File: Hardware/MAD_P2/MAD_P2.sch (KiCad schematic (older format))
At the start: 51 parts, among them U1 P2X8C4M64P-REF, Y1 20MHz

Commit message: added optional sd card socket for data
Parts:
- added SW?: Switch_SW_Push, symbol Power-cache:Switch_SW_Push
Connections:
- net GND: now also SW?.2
- net RESET: now also SW?.1
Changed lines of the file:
@@
 Text Notes 2950 2050 0    129  ~ 0
 Propeller 2
+$Comp
+L Power-cache:Switch_SW_Push SW?
+U 1 1 61238802
+P 3600 6750
+F 0 "SW?" H 3600 7035 50  0000 C CNN
+F 1 "Switch_SW_Push" H 3600 6944 50  0000 C CNN
+F 2 "" H 3600 6950 50  0001 C CNN
+F 3 "" H 3600 6950 50  0001 C CNN
+	1    3600 6750
+	1    0    0    -1
+$EndComp
+Text Label 3400 6750 2    50   ~ 0
+RESET
+$Comp
+L power:GND #PWR?
+U 1 1 6123970E
+P 3800 6750
+F 0 "#PWR?" H 3800 6500 50  0001 C CNN
+F 1 "GND" H 3805 6577 50  0000 C CNN
+F 2 "" H 3800 6750 50  0001 C CNN
+F 3 "" H 3800 6750 50  0001 C CNN
+	1    3800 6750
+	0    -1   -1   0
+$EndComp
 $EndSCHEMATC

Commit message: revising pcb layout
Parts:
- SW1: renamed from SW?; footprint (none) -> Button_Switch_THT:SW_PUSH_6mm
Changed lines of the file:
@@
 Propeller 2
 $Comp
-L Power-cache:Switch_SW_Push SW?
+L Power-cache:Switch_SW_Push SW1
 U 1 1 61238802
 P 3600 6750
-F 0 "SW?" H 3600 7035 50  0000 C CNN
+F 0 "SW1" H 3600 7035 50  0000 C CNN
 F 1 "Switch_SW_Push" H 3600 6944 50  0000 C CNN
-F 2 "" H 3600 6950 50  0001 C CNN
+F 2 "Button_Switch_THT:SW_PUSH_6mm" H 3600 6950 50  0001 C CNN
 F 3 "" H 3600 6950 50  0001 C CNN
 	1    3600 6750
@@
 RESET
 $Comp
-L power:GND #PWR?
+L power:GND #PWR0101
 U 1 1 6123970E
 P 3800 6750
-F 0 "#PWR?" H 3800 6500 50  0001 C CNN
+F 0 "#PWR0101" H 3800 6500 50  0001 C CNN
 F 1 "GND" H 3805 6577 50  0000 C CNN
 F 2 "" H 3800 6750 50  0001 C CNN

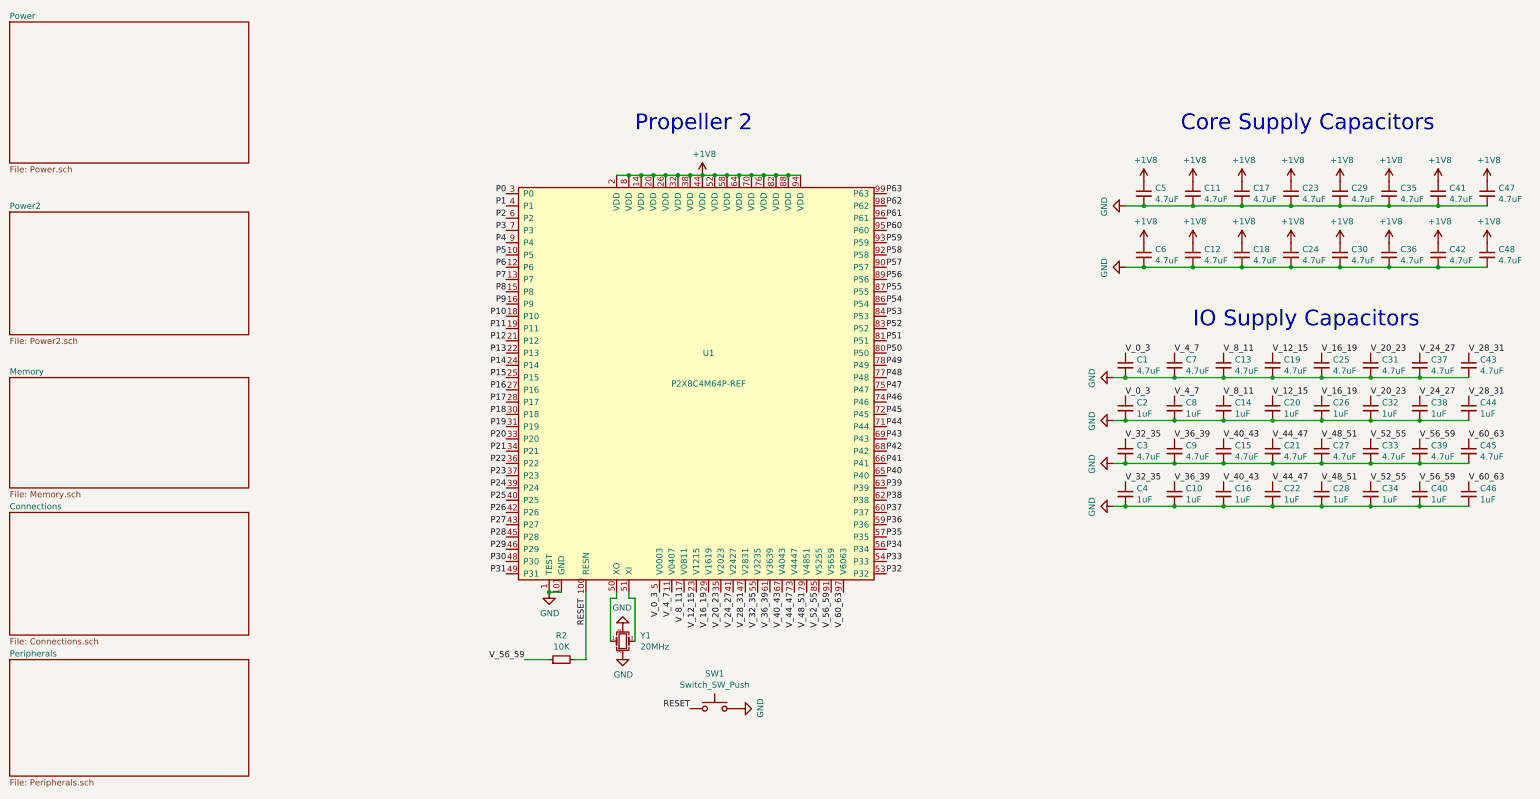
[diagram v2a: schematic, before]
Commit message: routed adc
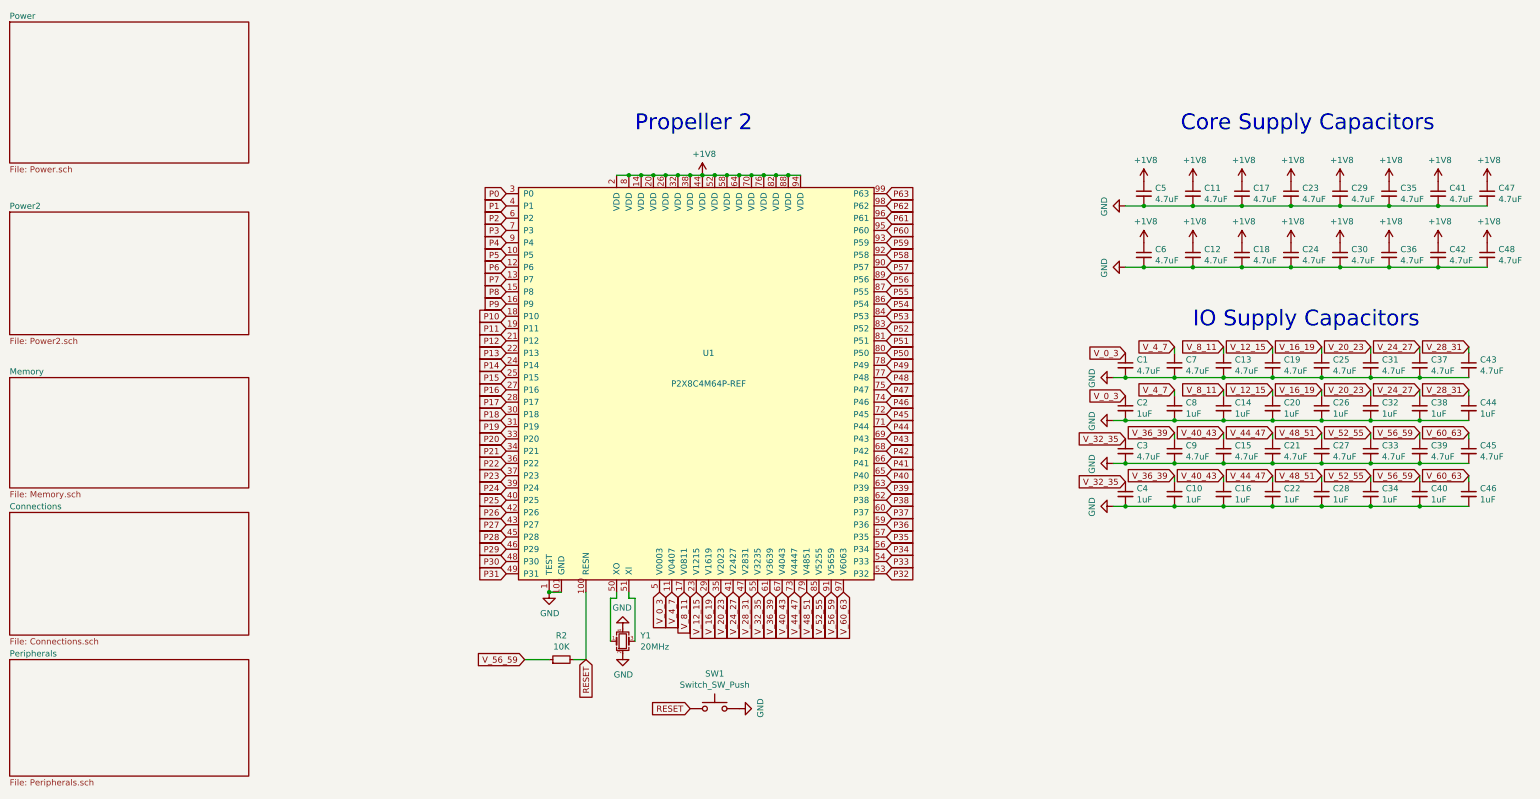
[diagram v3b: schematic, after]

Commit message: completed BOM with digikey and LSCS parts
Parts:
- C1, C11, C12, C13, C15, C17, C18, C19, C21, C23, C24, C25, C27, C29, C3, C30, C31, C33, C35, C36, C37, C39, C41, C42, C43, C45, C47, C48, C5, C6, C7, C9: LCSC (none) -> C19666; TYPE (none) -> BASIC
- C10, C14, C16, C2, C20, C22, C26, C28, C32, C34, C38, C4, C40, C44, C46, C8: LCSC (none) -> C15849; TYPE (none) -> BASIC
- R2: LCSC (none) -> C25804; TYPE (none) -> BASIC
- SW1: TYPE (none) -> NA
- U1: DIGIKEY (none) -> 149-P2X8C4M64P-ND; TYPE (none) -> DIGIKEY
- Y1: LCSC (none) -> C110936; TYPE (none) -> EXT

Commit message: added more functionality to JSON for motion quartet, motion set, motion profiles, machine profile, and more
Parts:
- C1, C10, C11, C12, C13, C14, C15, C16, C17, C18, C19, C2, C20, C21, C22, C23, C24, C25, C26, C27, C28, C29, C3, C30, C31, C32, C33, C34, C35, C36, C37, C38, C39, C4, C40, C41, C42, C43, C44, C45, C46, C47, C48, C5, C6, C7, C8, C9, R2: ASSEMBLED (none) -> YES
- U1, Y1: ASSEMBLED (none) -> NO
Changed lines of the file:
@@
 F 4 "149-P2X8C4M64P-ND" H 3550 4150 50  0001 C CNN "DIGIKEY"
 F 5 "DIGIKEY" H 3550 4150 50  0001 C CNN "TYPE"
+F 6 "NO" H 3550 4150 50  0001 C CNN "ASSEMBLED"
 	1    3550 4150
 	1    0    0    -1
@@
 F 4 "C110936" H 2850 6200 50  0001 C CNN "LCSC"
 F 5 "EXT" H 2850 6200 50  0001 C CNN "TYPE"
+F 6 "NO" H 2850 6200 50  0001 C CNN "ASSEMBLED"
 	1    2850 6200
 	1    0    0    -1
@@
 F 4 "C19666" H 7100 2550 50  0001 C CNN "LCSC"
 F 5 "BASIC" H 7100 2550 50  0001 C CNN "TYPE"
+F 6 "YES" H 7100 2550 50  0001 C CNN "ASSEMBLED"
 	1    7100 2550
 	1    0    0    -1
@@
 F 4 "C19666" H 7500 2550 50  0001 C CNN "LCSC"
 F 5 "BASIC" H 7500 2550 50  0001 C CNN "TYPE"
+F 6 "YES" H 7500 2550 50  0001 C CNN "ASSEMBLED"
 	1    7500 2550
 	1    0    0    -1
@@
 F 4 "C19666" H 7900 2550 50  0001 C CNN "LCSC"
 F 5 "BASIC" H 7900 2550 50  0001 C CNN "TYPE"
+F 6 "YES" H 7900 2550 50  0001 C CNN "ASSEMBLED"
 	1    7900 2550
 	1    0    0    -1
@@
 F 4 "C19666" H 8300 2550 50  0001 C CNN "LCSC"
 F 5 "BASIC" H 8300 2550 50  0001 C CNN "TYPE"
+F 6 "YES" H 8300 2550 50  0001 C CNN "ASSEMBLED"
 	1    8300 2550
 	1    0    0    -1
@@
 F 4 "C19666" H 8700 2550 50  0001 C CNN "LCSC"
 F 5 "BASIC" H 8700 2550 50  0001 C CNN "TYPE"
+F 6 "YES" H 8700 2550 50  0001 C CNN "ASSEMBLED"
 	1    8700 2550
 	1    0    0    -1
@@
 F 4 "C19666" H 9100 2550 50  0001 C CNN "LCSC"
 F 5 "BASIC" H 9100 2550 50  0001 C CNN "TYPE"
+F 6 "YES" H 9100 2550 50  0001 C CNN "ASSEMBLED"
 	1    9100 2550
 	1    0    0    -1
@@
 F 4 "C19666" H 9500 2550 50  0001 C CNN "LCSC"
 F 5 "BASIC" H 9500 2550 50  0001 C CNN "TYPE"
+F 6 "YES" H 9500 2550 50  0001 C CNN "ASSEMBLED"
 	1    9500 2550
 	1    0    0    -1
@@
 F 4 "C19666" H 9900 2550 50  0001 C CNN "LCSC"
 F 5 "BASIC" H 9900 2550 50  0001 C CNN "TYPE"
+F 6 "YES" H 9900 2550 50  0001 C CNN "ASSEMBLED"
 	1    9900 2550
 	1    0    0    -1
@@
 F 4 "C19666" H 7100 3050 50  0001 C CNN "LCSC"
 F 5 "BASIC" H 7100 3050 50  0001 C CNN "TYPE"
+F 6 "YES" H 7100 3050 50  0001 C CNN "ASSEMBLED"
 	1    7100 3050
 	1    0    0    -1
@@
 F 4 "C19666" H 7500 3050 50  0001 C CNN "LCSC"
 F 5 "BASIC" H 7500 3050 50  0001 C CNN "TYPE"
+F 6 "YES" H 7500 3050 50  0001 C CNN "ASSEMBLED"
 	1    7500 3050
 	1    0    0    -1
@@
 F 4 "C19666" H 7900 3050 50  0001 C CNN "LCSC"
 F 5 "BASIC" H 7900 3050 50  0001 C CNN "TYPE"
+F 6 "YES" H 7900 3050 50  0001 C CNN "ASSEMBLED"
 	1    7900 3050
 	1    0    0    -1
@@
 F 4 "C19666" H 8300 3050 50  0001 C CNN "LCSC"
 F 5 "BASIC" H 8300 3050 50  0001 C CNN "TYPE"
+F 6 "YES" H 8300 3050 50  0001 C CNN "ASSEMBLED"
 	1    8300 3050
 	1    0    0    -1
@@
 F 4 "C19666" H 8700 3050 50  0001 C CNN "LCSC"
 F 5 "BASIC" H 8700 3050 50  0001 C CNN "TYPE"
+F 6 "YES" H 8700 3050 50  0001 C CNN "ASSEMBLED"
 	1    8700 3050
 	1    0    0    -1
@@
 F 4 "C19666" H 9100 3050 50  0001 C CNN "LCSC"
 F 5 "BASIC" H 9100 3050 50  0001 C CNN "TYPE"
+F 6 "YES" H 9100 3050 50  0001 C CNN "ASSEMBLED"
 	1    9100 3050
 	1    0    0    -1
@@
 F 4 "C19666" H 9500 3050 50  0001 C CNN "LCSC"
 F 5 "BASIC" H 9500 3050 50  0001 C CNN "TYPE"
+F 6 "YES" H 9500 3050 50  0001 C CNN "ASSEMBLED"
 	1    9500 3050
 	1    0    0    -1
@@
 F 4 "C19666" H 9900 3050 50  0001 C CNN "LCSC"
 F 5 "BASIC" H 9900 3050 50  0001 C CNN "TYPE"
+F 6 "YES" H 9900 3050 50  0001 C CNN "ASSEMBLED"
 	1    9900 3050
 	1    0    0    -1
@@
 F 4 "C19666" H 6950 3950 50  0001 C CNN "LCSC"
 F 5 "BASIC" H 6950 3950 50  0001 C CNN "TYPE"
+F 6 "YES" H 6950 3950 50  0001 C CNN "ASSEMBLED"
 	1    6950 3950
 	1    0    0    -1
@@
 F 4 "C19666" H 7350 3950 50  0001 C CNN "LCSC"
 F 5 "BASIC" H 7350 3950 50  0001 C CNN "TYPE"
+F 6 "YES" H 7350 3950 50  0001 C CNN "ASSEMBLED"
 	1    7350 3950
 	1    0    0    -1
@@
 F 4 "C19666" H 7750 3950 50  0001 C CNN "LCSC"
 F 5 "BASIC" H 7750 3950 50  0001 C CNN "TYPE"
+F 6 "YES" H 7750 3950 50  0001 C CNN "ASSEMBLED"
 	1    7750 3950
 	1    0    0    -1
@@
 F 4 "C19666" H 8150 3950 50  0001 C CNN "LCSC"
 F 5 "BASIC" H 8150 3950 50  0001 C CNN "TYPE"
+F 6 "YES" H 8150 3950 50  0001 C CNN "ASSEMBLED"
 	1    8150 3950
 	1    0    0    -1
@@
 F 4 "C19666" H 8550 3950 50  0001 C CNN "LCSC"
 F 5 "BASIC" H 8550 3950 50  0001 C CNN "TYPE"
+F 6 "YES" H 8550 3950 50  0001 C CNN "ASSEMBLED"
 	1    8550 3950
 	1    0    0    -1
@@
 F 4 "C19666" H 8950 3950 50  0001 C CNN "LCSC"
 F 5 "BASIC" H 8950 3950 50  0001 C CNN "TYPE"
+F 6 "YES" H 8950 3950 50  0001 C CNN "ASSEMBLED"
 	1    8950 3950
 	1    0    0    -1
@@
 F 4 "C19666" H 9350 3950 50  0001 C CNN "LCSC"
 F 5 "BASIC" H 9350 3950 50  0001 C CNN "TYPE"
+F 6 "YES" H 9350 3950 50  0001 C CNN "ASSEMBLED"
 	1    9350 3950
 	1    0    0    -1
@@
 F 4 "C19666" H 9750 3950 50  0001 C CNN "LCSC"
 F 5 "BASIC" H 9750 3950 50  0001 C CNN "TYPE"
+F 6 "YES" H 9750 3950 50  0001 C CNN "ASSEMBLED"
 	1    9750 3950
 	1    0    0    -1
@@
 F 4 "C19666" H 6950 4650 50  0001 C CNN "LCSC"
 F 5 "BASIC" H 6950 4650 50  0001 C CNN "TYPE"
+F 6 "YES" H 6950 4650 50  0001 C CNN "ASSEMBLED"
 	1    6950 4650
 	1    0    0    -1
@@
 F 4 "C19666" H 7350 4650 50  0001 C CNN "LCSC"
 F 5 "BASIC" H 7350 4650 50  0001 C CNN "TYPE"
+F 6 "YES" H 7350 4650 50  0001 C CNN "ASSEMBLED"
 	1    7350 4650
 	1    0    0    -1
@@
 F 4 "C19666" H 7750 4650 50  0001 C CNN "LCSC"
 F 5 "BASIC" H 7750 4650 50  0001 C CNN "TYPE"
+F 6 "YES" H 7750 4650 50  0001 C CNN "ASSEMBLED"
 	1    7750 4650
 	1    0    0    -1
@@
 F 4 "C19666" H 8150 4650 50  0001 C CNN "LCSC"
 F 5 "BASIC" H 8150 4650 50  0001 C CNN "TYPE"
+F 6 "YES" H 8150 4650 50  0001 C CNN "ASSEMBLED"
 	1    8150 4650
 	1    0    0    -1
@@
 F 4 "C19666" H 8550 4650 50  0001 C CNN "LCSC"
 F 5 "BASIC" H 8550 4650 50  0001 C CNN "TYPE"
+F 6 "YES" H 8550 4650 50  0001 C CNN "ASSEMBLED"
 	1    8550 4650
 	1    0    0    -1
@@
 F 4 "C19666" H 8950 4650 50  0001 C CNN "LCSC"
 F 5 "BASIC" H 8950 4650 50  0001 C CNN "TYPE"
+F 6 "YES" H 8950 4650 50  0001 C CNN "ASSEMBLED"
 	1    8950 4650
 	1    0    0    -1
@@
 F 4 "C19666" H 9350 4650 50  0001 C CNN "LCSC"
 F 5 "BASIC" H 9350 4650 50  0001 C CNN "TYPE"
+F 6 "YES" H 9350 4650 50  0001 C CNN "ASSEMBLED"
 	1    9350 4650
 	1    0    0    -1
@@
 F 4 "C19666" H 9750 4650 50  0001 C CNN "LCSC"
 F 5 "BASIC" H 9750 4650 50  0001 C CNN "TYPE"
+F 6 "YES" H 9750 4650 50  0001 C CNN "ASSEMBLED"
 	1    9750 4650
 	1    0    0    -1
@@
 F 4 "C15849" H 6950 5000 50  0001 C CNN "LCSC"
 F 5 "BASIC" H 6950 5000 50  0001 C CNN "TYPE"
+F 6 "YES" H 6950 5000 50  0001 C CNN "ASSEMBLED"
 	1    6950 5000
 	1    0    0    -1
@@
 F 4 "C15849" H 7350 5000 50  0001 C CNN "LCSC"
 F 5 "BASIC" H 7350 5000 50  0001 C CNN "TYPE"
+F 6 "YES" H 7350 5000 50  0001 C CNN "ASSEMBLED"
 	1    7350 5000
 	1    0    0    -1
@@
 F 4 "C15849" H 7750 5000 50  0001 C CNN "LCSC"
 F 5 "BASIC" H 7750 5000 50  0001 C CNN "TYPE"
+F 6 "YES" H 7750 5000 50  0001 C CNN "ASSEMBLED"
 	1    7750 5000
 	1    0    0    -1
@@
 F 4 "C15849" H 8150 5000 50  0001 C CNN "LCSC"
 F 5 "BASIC" H 8150 5000 50  0001 C CNN "TYPE"
+F 6 "YES" H 8150 5000 50  0001 C CNN "ASSEMBLED"
 	1    8150 5000
 	1    0    0    -1
@@
 F 4 "C15849" H 8550 5000 50  0001 C CNN "LCSC"
 F 5 "BASIC" H 8550 5000 50  0001 C CNN "TYPE"
+F 6 "YES" H 8550 5000 50  0001 C CNN "ASSEMBLED"
 	1    8550 5000
 	1    0    0    -1
@@
 F 4 "C15849" H 8950 5000 50  0001 C CNN "LCSC"
 F 5 "BASIC" H 8950 5000 50  0001 C CNN "TYPE"
+F 6 "YES" H 8950 5000 50  0001 C CNN "ASSEMBLED"
 	1    8950 5000
 	1    0    0    -1
@@
 F 4 "C15849" H 9350 5000 50  0001 C CNN "LCSC"
 F 5 "BASIC" H 9350 5000 50  0001 C CNN "TYPE"
+F 6 "YES" H 9350 5000 50  0001 C CNN "ASSEMBLED"
 	1    9350 5000
 	1    0    0    -1
@@
 F 4 "C15849" H 9750 5000 50  0001 C CNN "LCSC"
 F 5 "BASIC" H 9750 5000 50  0001 C CNN "TYPE"
+F 6 "YES" H 9750 5000 50  0001 C CNN "ASSEMBLED"
 	1    9750 5000
 	1    0    0    -1
@@
 F 4 "C15849" H 6950 4300 50  0001 C CNN "LCSC"
 F 5 "BASIC" H 6950 4300 50  0001 C CNN "TYPE"
+F 6 "YES" H 6950 4300 50  0001 C CNN "ASSEMBLED"
 	1    6950 4300
 	1    0    0    -1
@@
 F 4 "C15849" H 7350 4300 50  0001 C CNN "LCSC"
 F 5 "BASIC" H 7350 4300 50  0001 C CNN "TYPE"
+F 6 "YES" H 7350 4300 50  0001 C CNN "ASSEMBLED"
 	1    7350 4300
 	1    0    0    -1
@@
 F 4 "C15849" H 7750 4300 50  0001 C CNN "LCSC"
 F 5 "BASIC" H 7750 4300 50  0001 C CNN "TYPE"
+F 6 "YES" H 7750 4300 50  0001 C CNN "ASSEMBLED"
 	1    7750 4300
 	1    0    0    -1
@@
 F 4 "C15849" H 8150 4300 50  0001 C CNN "LCSC"
 F 5 "BASIC" H 8150 4300 50  0001 C CNN "TYPE"
+F 6 "YES" H 8150 4300 50  0001 C CNN "ASSEMBLED"
 	1    8150 4300
 	1    0    0    -1
@@
 F 4 "C15849" H 8550 4300 50  0001 C CNN "LCSC"
 F 5 "BASIC" H 8550 4300 50  0001 C CNN "TYPE"
+F 6 "YES" H 8550 4300 50  0001 C CNN "ASSEMBLED"
 	1    8550 4300
 	1    0    0    -1
@@
 F 4 "C15849" H 8950 4300 50  0001 C CNN "LCSC"
 F 5 "BASIC" H 8950 4300 50  0001 C CNN "TYPE"
+F 6 "YES" H 8950 4300 50  0001 C CNN "ASSEMBLED"
 	1    8950 4300
 	1    0    0    -1
@@
 F 4 "C15849" H 9350 4300 50  0001 C CNN "LCSC"
 F 5 "BASIC" H 9350 4300 50  0001 C CNN "TYPE"
+F 6 "YES" H 9350 4300 50  0001 C CNN "ASSEMBLED"
 	1    9350 4300
 	1    0    0    -1
@@
 F 4 "C15849" H 9750 4300 50  0001 C CNN "LCSC"
 F 5 "BASIC" H 9750 4300 50  0001 C CNN "TYPE"
+F 6 "YES" H 9750 4300 50  0001 C CNN "ASSEMBLED"
 	1    9750 4300
 	1    0    0    -1
@@
 F 4 "C25804" H 2350 6350 50  0001 C CNN "LCSC"
 F 5 "BASIC" H 2350 6350 50  0001 C CNN "TYPE"
+F 6 "YES" H 2350 6350 50  0001 C CNN "ASSEMBLED"
 	1    2350 6350
 	0    -1   -1   0
